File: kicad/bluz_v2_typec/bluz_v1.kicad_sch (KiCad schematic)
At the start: 75 parts, among them J10 Conn, J11 Conn, J12 BTAnt, J2 Conn, J3 Conn, J4 Conn, J5 Conn, J6 Conn, J7 Conn, J8 Conn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

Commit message: изменено:      kicad/bluz_v2_typec/bluz_v1.kicad_pcb 	изменено:      kicad/bluz_v2_typec/bluz_v1.kicad_prl 	изменено:      kicad/bluz_v2_typec/bluz_v1.kicad_pro 	изменено:      kicad/bluz_v2_typec/bluz_v1.kicad_sch
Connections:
- net Rst: now reaches C18.2, D1.24 (RST), J2.1
- net 1.8v: now reaches C23.1, C8.1, D1.5 (VDA), U5.2 (VO)
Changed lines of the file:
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@@
+	)
+	(junction
+		(at 77.47 81.915)
+		(diameter 0)
+		(color 0 0 0 0)
 	)
 	(junction
@@
 	(wire
 		(pts
+			(xy 80.01 78.74) (xy 77.47 78.74)
+		)
+		(stroke
+			(width 0)
+			(type default)
+		)
+	)
+	(wire
+		(pts
+			(xy 77.47 78.74) (xy 77.47 81.915)
+		)
+		(stroke
+			(width 0)
+			(type default)
+		)
+	)
+	(wire
+		(pts
 			(xy 179.07 102.87) (xy 179.07 107.95)
 		)
@@
 	(label "swd"
 		(at 73.66 123.19 0)
+		(effects
+			(font
+				(size 1.27 1.27)
+			)
+			(justify left bottom)
+		)
+	)
+	(label "1.8v"
+		(at 109.22 62.23 0)
 		(effects
 			(font
@@
 			(effects
 				(font
+					(size 1.27 1.27)
+				)
+				(justify left)
+				(hide yes)
+			)
+		)
+	)
+	(global_label "Rst"
+		(shape input)
+		(at 80.01 78.74 0)
+		(fields_autoplaced yes)
+		(effects
+			(font
+				(size 1.27 1.27)
+			)
+			(justify left)
+		)
+		(property "Intersheetrefs" "${INTERSHEET_REFS}"
+			(at 86.019 78.74 0)
+			(effects
+				(font

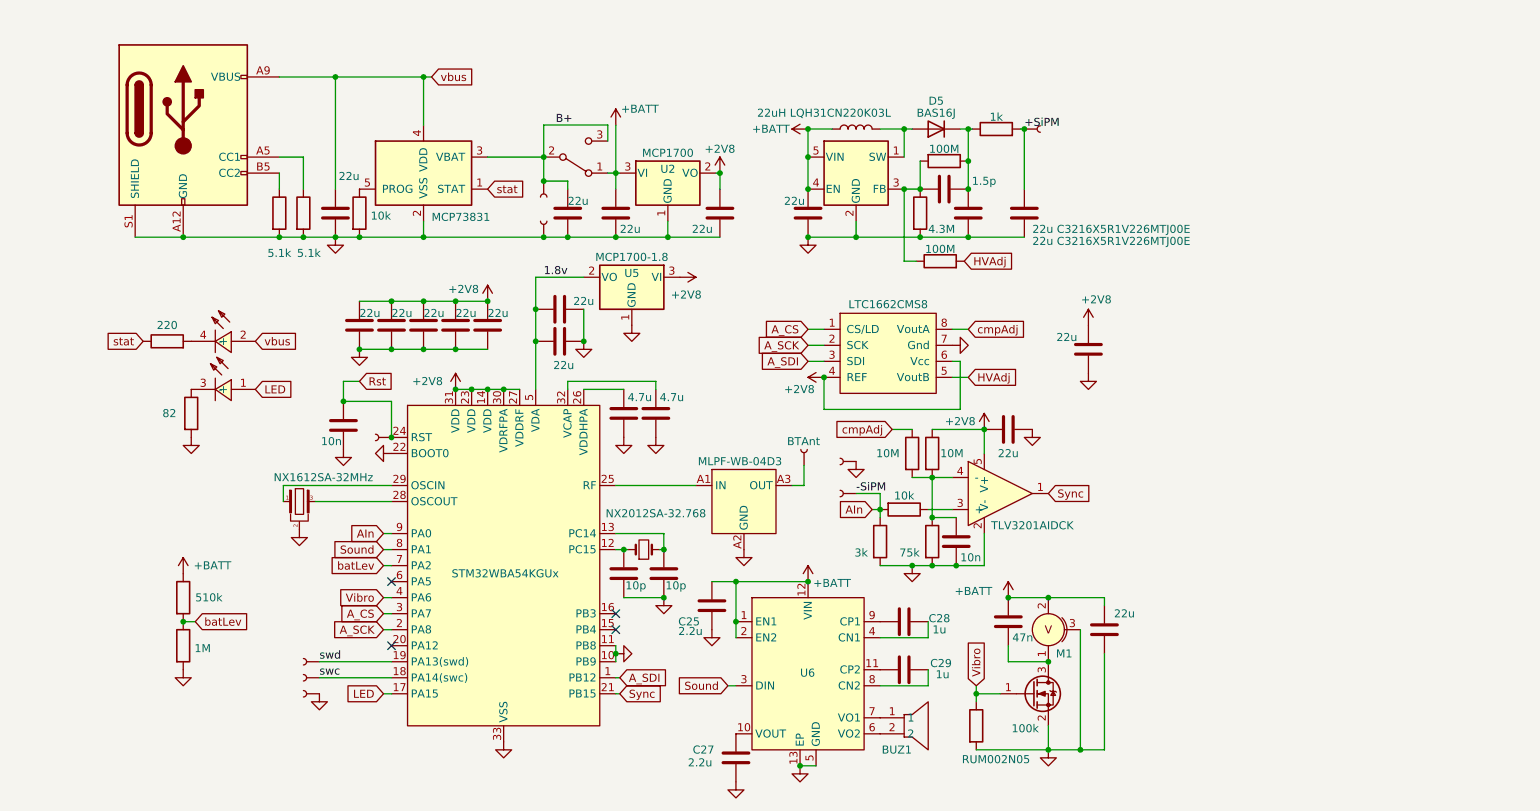
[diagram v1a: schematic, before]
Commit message: изменено:      Android/BluZ_LPM/BluZ/src/main/java/ru/starline/bluz/BluetoothInterface.kt 	удалено:       kicad/bluz_v2_typec/bluz_v1-backups/bluz_v1-2025-11-25_164259.zip 	удалено:       kicad/bluz_v2_typec/bluz_v1-backups/bluz_v1-2025-11-25_165421.zip 	удалено:       kicad/bluz_v2_typec/bluz_v1-backups/bluz_v1-2025-11-29_144245.zip 	удалено:       kicad/bluz_v2_typec/bluz_v1-backups/bluz_v1-2026-01-22_200222.zip 	изменено:      kicad/bluz_v2_typec/bluz_v1.kicad_pcb 	изменено:      kicad/bluz_v2_typec/bluz_v1.kicad_prl 	изменено:      kicad/bluz_v2_typec/bluz_v1.kicad_sch 	изменено:      stm32cubeide/BluZ_LPM/BluZ_LPM_v1.ioc 	изменено:      stm32cubeide/BluZ_LPM/Core/Src/main.c 	изменено:      stm32cubeide/BluZ_LPM/Release/BluZ_LPM_v1.elf 	изменено:      stm32cubeide/BluZ_archive/.settings/language.settings.xml
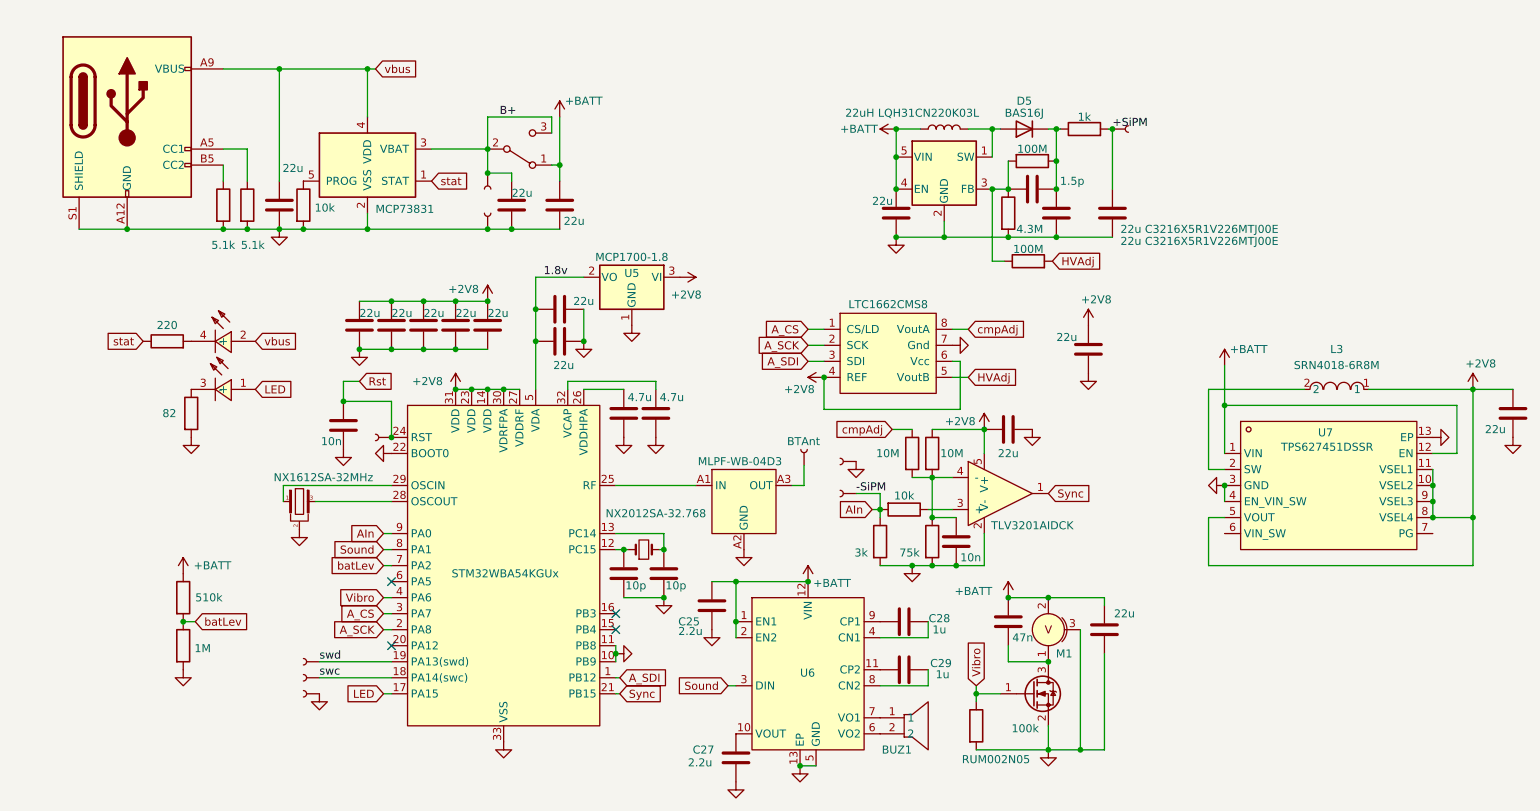
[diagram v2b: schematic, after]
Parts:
- removed U2: MCP1700, Package_TO_SOT_SMD:SOT-23-3, symbol Regulator_Linear:MCP1700x-280xxTT
- added L3: SRN4018-6R8M, easyeda2kicad:IND-SMD_L4.0-W4.0_SMNR4018, symbol easyeda2kicad:SRN4018-6R8M
- added U7: TPS627451DSSR, easyeda2kicad:WSON-12_L3.0-W2.0-P0.5-BL-EP, symbol easyeda2kicad:TPS627451DSSR
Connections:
- net +2V8: now also L3.1, U7.10 (VSEL2), U7.11 (VSEL1), U7.5 (VOUT), U7.8 (VSEL4), U7.9 (VSEL3)
- net +BATT: now also U7.1 (VIN), U7.12 (EN)
- net GND: now also U7.13 (EP), U7.3 (GND), U7.4 (EN_VIN_SW)
- new net: L3.2, U7.2 (SW)
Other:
- moved on the sheet: D5

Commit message: удалено:       kicad/bluz_v2_typec/bluz_v1-backups/bluz_v1-2026-01-23_152519.zip 	изменено:      kicad/bluz_v2_typec/bluz_v1.kicad_pcb 	изменено:      kicad/bluz_v2_typec/bluz_v1.kicad_prl 	изменено:      kicad/bluz_v2_typec/bluz_v1.kicad_pro 	изменено:      kicad/bluz_v2_typec/bluz_v1.kicad_sch
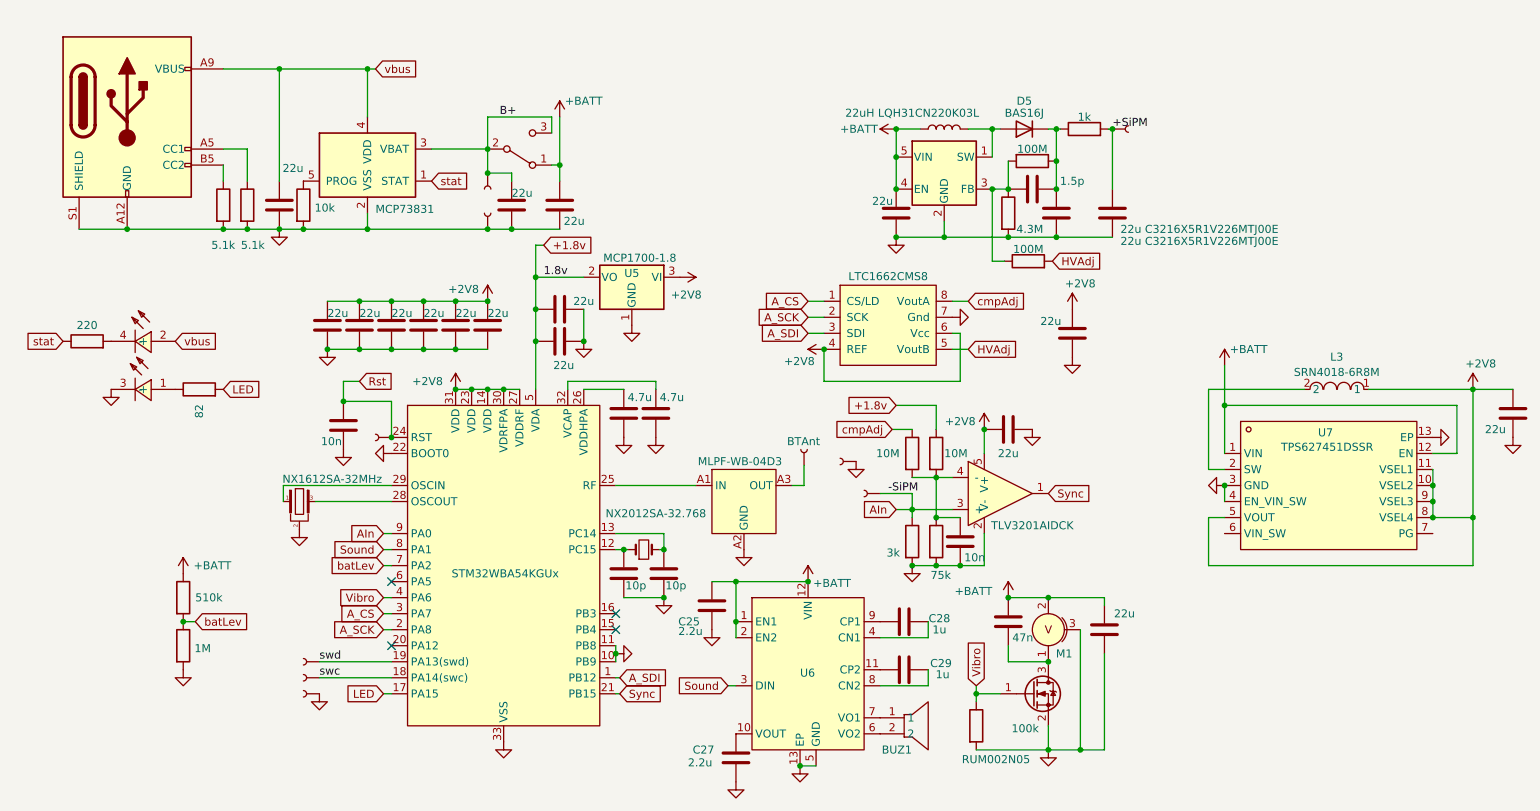
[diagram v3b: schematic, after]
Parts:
- removed R7: 10k, Resistor_SMD:R_0402_1005Metric, symbol Device:R
- added C30: 22u, Capacitor_SMD:C_0402_1005Metric, symbol Device:C
- L3: footprint easyeda2kicad:IND-SMD_L4.0-W4.0_SMNR4018 -> Inductor_SMD:L_1206_3216Metric_Pad1.42x1.75mm_HandSolder
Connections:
- net +2V8: now also C30.1; no longer R9.1
- net AIn: now also U3.3 (+)
- net GND: now also LED1.3 (-), C30.2; no longer R5.2
- net LED: now also R5.2; no longer LED1.1 (+)
- net at R5.1: now also LED1.1 (+); no longer LED1.3 (-)
- net 1.8v renamed +1.8v
- net +1.8v: now also R9.1

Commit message: изменено:      kicad/bluz_v2_typec/bluz_v1.kicad_prl 	изменено:      kicad/bluz_v2_typec/bluz_v1.kicad_sch
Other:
- moved on the sheet: D5, L3, U7

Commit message: изменено:      kicad/bluz_v2_typec/bluz_v1.kicad_pcb 	изменено:      kicad/bluz_v2_typec/bluz_v1.kicad_sch 	изменено:      kicad/bluz_v2_typec/fp-info-cache
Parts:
- L3: value SRN4018-6R8M -> LQH31MN5R6J03L
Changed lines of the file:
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@@
 		(on_board yes)
 		(dnp no)
-		(fields_autoplaced yes)
 		(property "Reference" "L3"
-			(at 143.51 22.797 0)
+			(at 143.256 23.114 0)
 			(effects
 				(font
@@
 			)
 		)
-		(property "Value" "SRN4018-6R8M"
-			(at 143.51 25.2213 0)
+		(property "Value" "LQH31MN5R6J03L"
+			(at 143.764 25.146 0)
 			(effects
 				(font
